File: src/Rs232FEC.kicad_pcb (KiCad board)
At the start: 2 copper layers, 24 x 27.9 mm, 25 parts, among them J1 B3B-XH-A, P1 105444-0001, Q1 DMP3099L-13, U1 FT232RL, U2 MAX232IDR

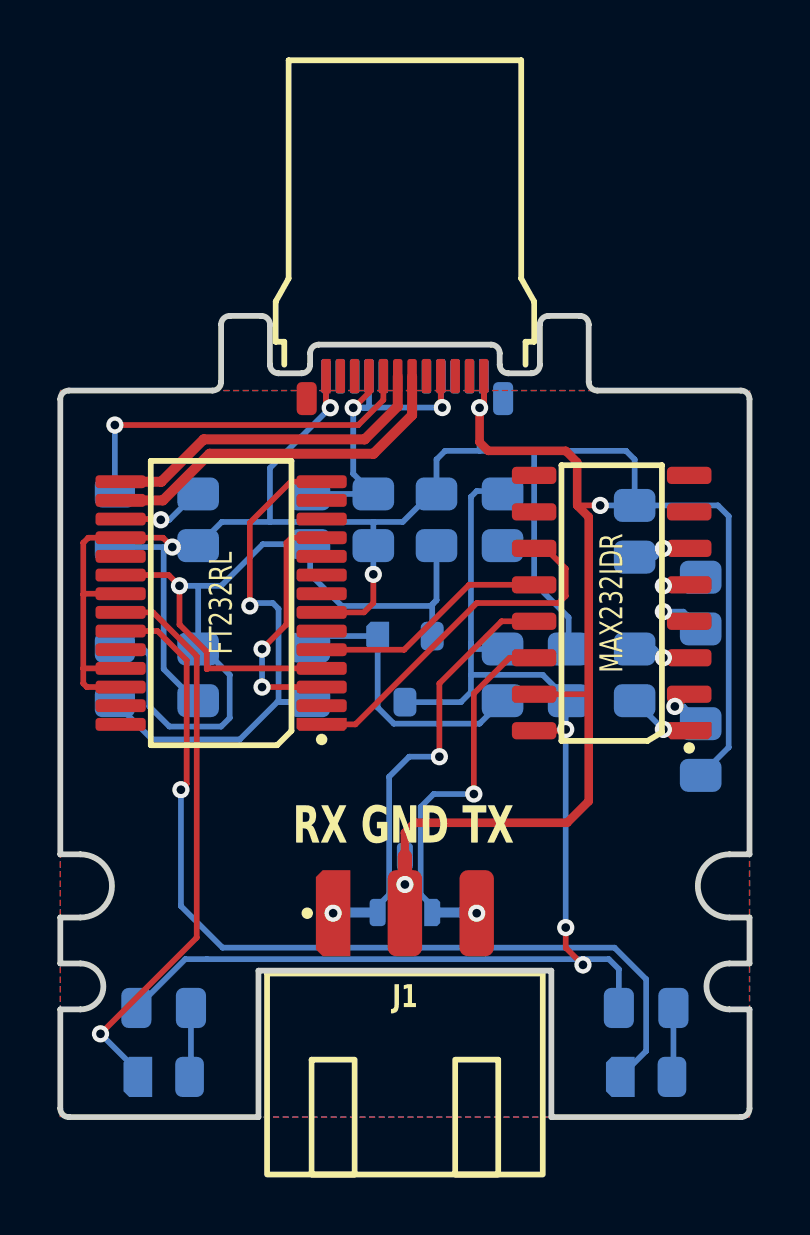
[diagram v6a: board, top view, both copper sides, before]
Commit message: Changed connector to include CTS/RTS lines
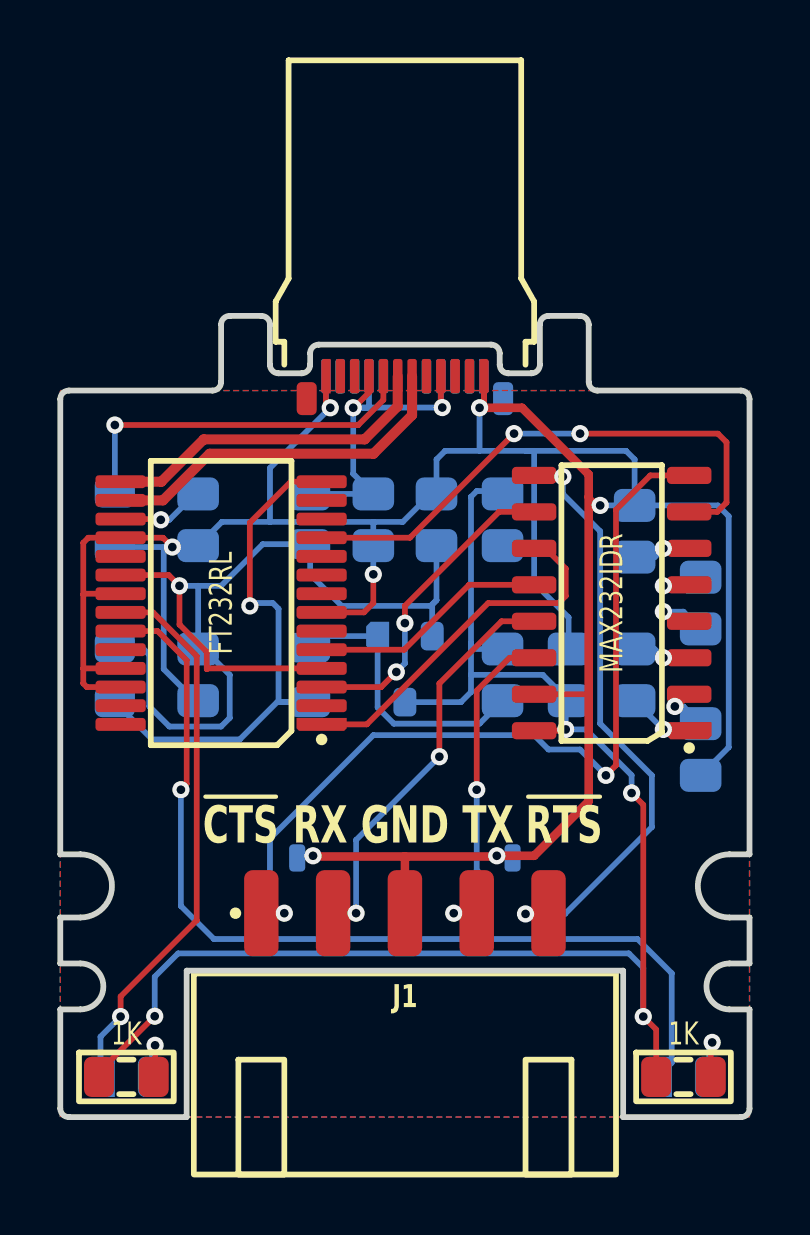
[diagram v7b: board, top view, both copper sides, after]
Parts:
- added D2: PESD12VL2BT, Medo64:D TVS SM05T1G (SOT23-3), B.Cu at (35.8, 39.9)
- J1: value B3B-XH-A -> B5B-XH-A; footprint Medo64:J JST XH Edge [UART] (3w) -> Medo64:J JST XH Edge [UART] (5w)
- R1, R2: moved to F.Cu
- moved D1 3.75 mm to (28.2, 39.9)
- moved R2 2.73 mm to (41.7, 46.5)
- moved R1 2.73 mm to (22.3, 46.5)
- moved DS2 1.30 mm to (41.7, 46.5)
- moved DS1 1.30 mm to (22.3, 46.5)
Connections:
- D1 pad 1: RS232_TX -> RS232_RX
- D1 pad 2: RS232_RX -> RS232_CTS
- J1 pad 1: RS232_RX -> RS232_CTS
- J1 pad 2: GND -> RS232_RX
- J1 pad 3: RS232_TX -> GND
- U1 pad 11: RTS_CTS -> CTS
- U1 pad 3: RTS_CTS -> RTS
- U2 pad 10: (no net) -> RTS
- U2 pad 7: (no net) -> CTS
- U2 pad 8: (no net) -> RS232_CTS
- U2 pad 9: (no net) -> RS232_RTS
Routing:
- net RS232_CTS: track 0.00 -> 30.6 mm, vias 0 -> 2
- net RS232_RTS: track 0.00 -> 21.1 mm, vias 0 -> 2
- net CTS: track 0.00 -> 19.3 mm, vias 0 -> 2
- net RTS: track 0.00 -> 11.1 mm, vias 0 -> 2
- net 5V_SW: track 45.5 -> 54.8 mm, vias 3 -> 4
- net RTS_CTS: track 8.75 -> 0.00 mm, vias 2 -> 0
- net GND: track 111.5 -> 112.8 mm, vias 6 -> 7
- net RS232_TX: track 13.3 -> 12.3 mm
- net LED_TXD: track 32.4 -> 33.2 mm
- net LED_TXD': track 2.35 -> 2.46 mm, vias 0 -> 1
- net LED_RXD': track 2.35 -> 2.26 mm, vias 0 -> 1
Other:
- outline, holes or cut-outs redrawn
- board text added: "~{CTS}"
- board text added: "~{RTS}"

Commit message: Moved LED resistors to bottom
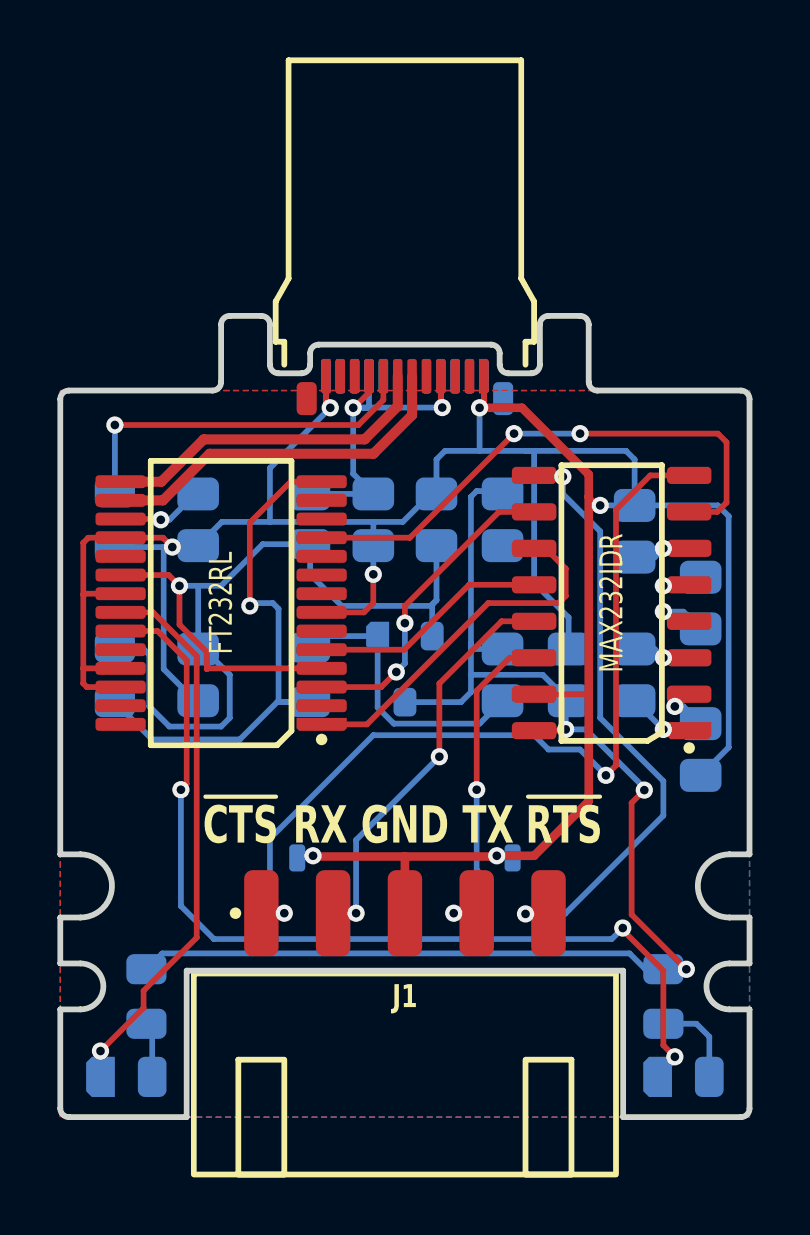
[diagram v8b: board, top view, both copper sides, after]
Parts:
- R1, R2: moved to B.Cu
- moved R2 2.89 mm to (41.0, 43.7), turned to -90 degrees
- moved R1 2.89 mm to (23.0, 43.7), turned to -90 degrees
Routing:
- net 5V_SW: track 54.8 -> 47.5 mm, vias 4 -> 3
- net LED_TXD': track 2.46 -> 3.19 mm, vias 1 -> 0
- net LED_RXD': track 2.26 -> 1.65 mm, vias 1 -> 0
- net LED_TXD: track 33.2 -> 33.6 mm, vias 1 -> 3
